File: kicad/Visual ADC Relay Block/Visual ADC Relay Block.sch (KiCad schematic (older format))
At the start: 34 parts, among them J1 Out, J2 In, K1 DIPxx-1Cxx-51x, Q1 P-NMOS, U1 74HCT595, U2 74HC245

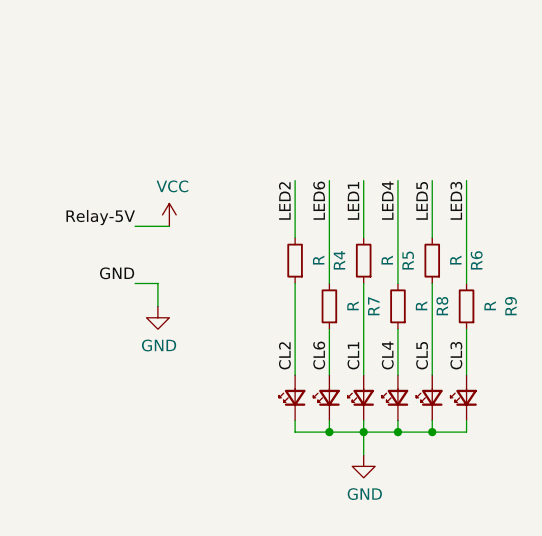
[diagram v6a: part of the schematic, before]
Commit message: rev1 boards tested
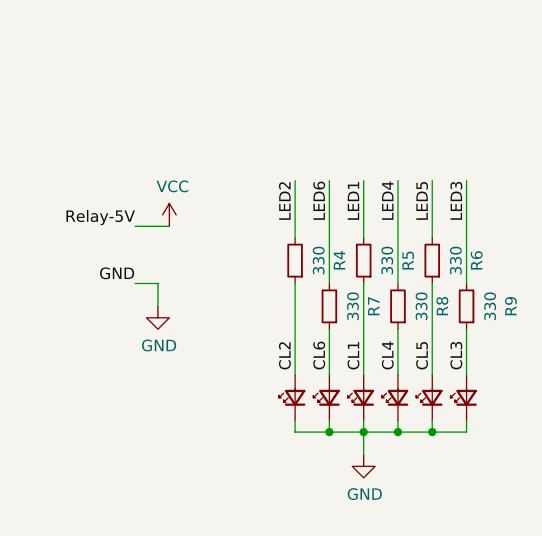
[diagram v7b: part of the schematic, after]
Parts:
- R4, R5, R6, R7, R8, R9: value R -> 330
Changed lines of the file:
@@
 P 14750 8750
 F 0 "R4" V 14554 8750 50  0000 C CNN
-F 1 "R" V 14645 8750 50  0000 C CNN
+F 1 "330" V 14645 8750 50  0000 C CNN
 F 2 "Resistor_SMD:R_0805_2012Metric_Pad1.20x1.40mm_HandSolder" H 14750 8750 50  0001 C CNN
 F 3 "~" H 14750 8750 50  0001 C CNN
@@
 P 14900 8950
 F 0 "R7" V 14704 8950 50  0000 C CNN
-F 1 "R" V 14795 8950 50  0000 C CNN
+F 1 "330" V 14795 8950 50  0000 C CNN
 F 2 "Resistor_SMD:R_0805_2012Metric_Pad1.20x1.40mm_HandSolder" H 14900 8950 50  0001 C CNN
 F 3 "~" H 14900 8950 50  0001 C CNN
@@
 P 15050 8750
 F 0 "R5" V 14854 8750 50  0000 C CNN
-F 1 "R" V 14945 8750 50  0000 C CNN
+F 1 "330" V 14945 8750 50  0000 C CNN
 F 2 "Resistor_SMD:R_0805_2012Metric_Pad1.20x1.40mm_HandSolder" H 15050 8750 50  0001 C CNN
 F 3 "~" H 15050 8750 50  0001 C CNN
@@
 P 15200 8950
 F 0 "R8" V 15004 8950 50  0000 C CNN
-F 1 "R" V 15095 8950 50  0000 C CNN
+F 1 "330" V 15095 8950 50  0000 C CNN
 F 2 "Resistor_SMD:R_0805_2012Metric_Pad1.20x1.40mm_HandSolder" H 15200 8950 50  0001 C CNN
 F 3 "~" H 15200 8950 50  0001 C CNN
@@
 P 15350 8750
 F 0 "R6" V 15154 8750 50  0000 C CNN
-F 1 "R" V 15245 8750 50  0000 C CNN
+F 1 "330" V 15245 8750 50  0000 C CNN
 F 2 "Resistor_SMD:R_0805_2012Metric_Pad1.20x1.40mm_HandSolder" H 15350 8750 50  0001 C CNN
 F 3 "~" H 15350 8750 50  0001 C CNN
@@
 P 15500 8950
 F 0 "R9" V 15304 8950 50  0000 C CNN
-F 1 "R" V 15395 8950 50  0000 C CNN
+F 1 "330" V 15395 8950 50  0000 C CNN
 F 2 "Resistor_SMD:R_0805_2012Metric_Pad1.20x1.40mm_HandSolder" H 15500 8950 50  0001 C CNN
 F 3 "~" H 15500 8950 50  0001 C CNN

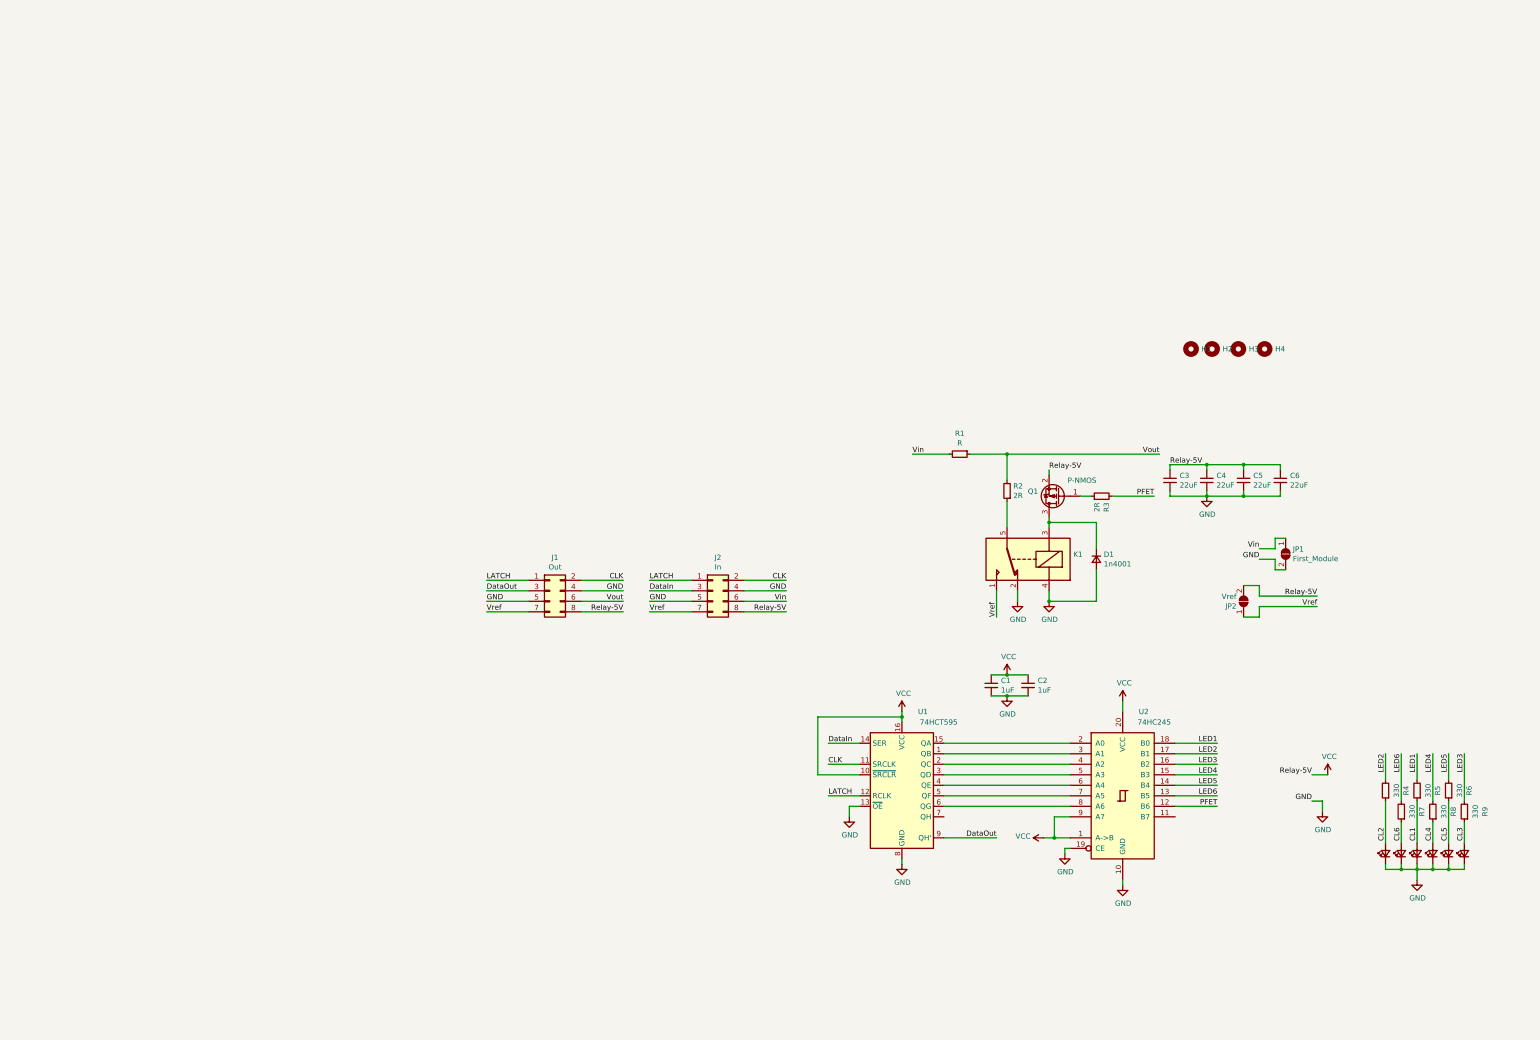
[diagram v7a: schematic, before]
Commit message: KiCad Notes and Clean-up
Finalized a few details on the schematic. Also created notes for each block based on experience building the boards.
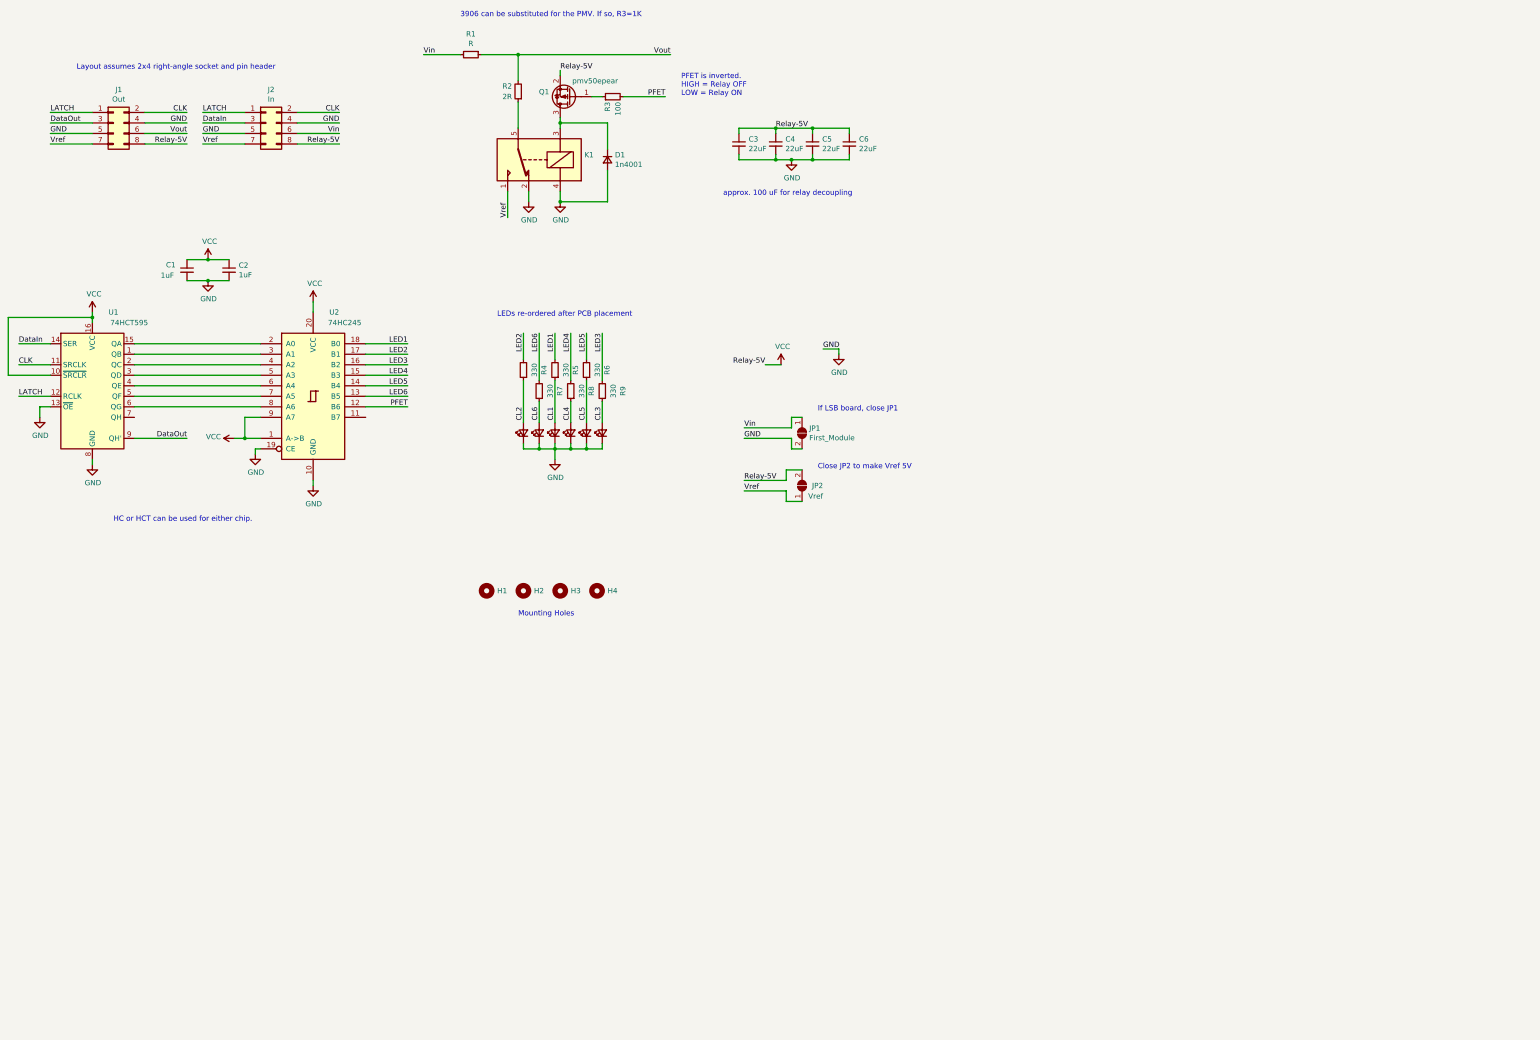
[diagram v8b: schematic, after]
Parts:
- Q1: value P-NMOS -> pmv50epear
- R3: value 2R -> 100
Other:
- note added: "3906 can be substituted for the PMV. If so, R3=1K"
- note added: "Close JP2 to make Vref 5V"
- note added: "HC or HCT can be used for either chip."
- note added: "If LSB board, close JP1"
- note added: "LEDs re-ordered after PCB placement"
- note added: "Layout assumes 2x4 right-angle socket and pin header"
- note added: "Mounting Holes"
- note added: "PFET is inverted.\nHIGH = Relay OFF\nLOW = Relay ON"
- note added: "approx. 100 uF for relay decoupling"
- moved on the sheet: C1, C2, C3, C4, C5, C6, D1, H1, H2, H3, H4, J1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
